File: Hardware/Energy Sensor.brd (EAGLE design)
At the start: 159 x 63 mm, 41 parts, among them Q1 16MHz

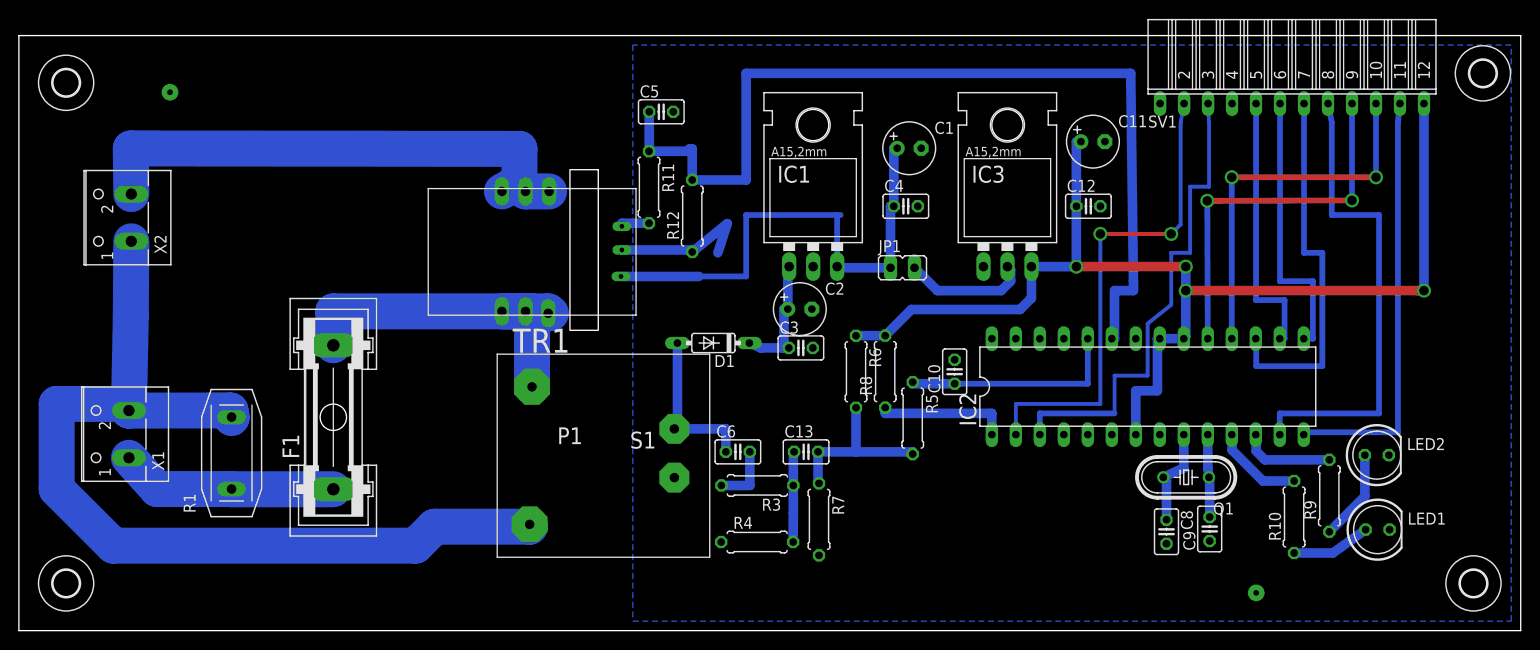
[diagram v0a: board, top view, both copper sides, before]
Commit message: update schematics, added switchmode psu to heating controller. fixed line endings for existing files
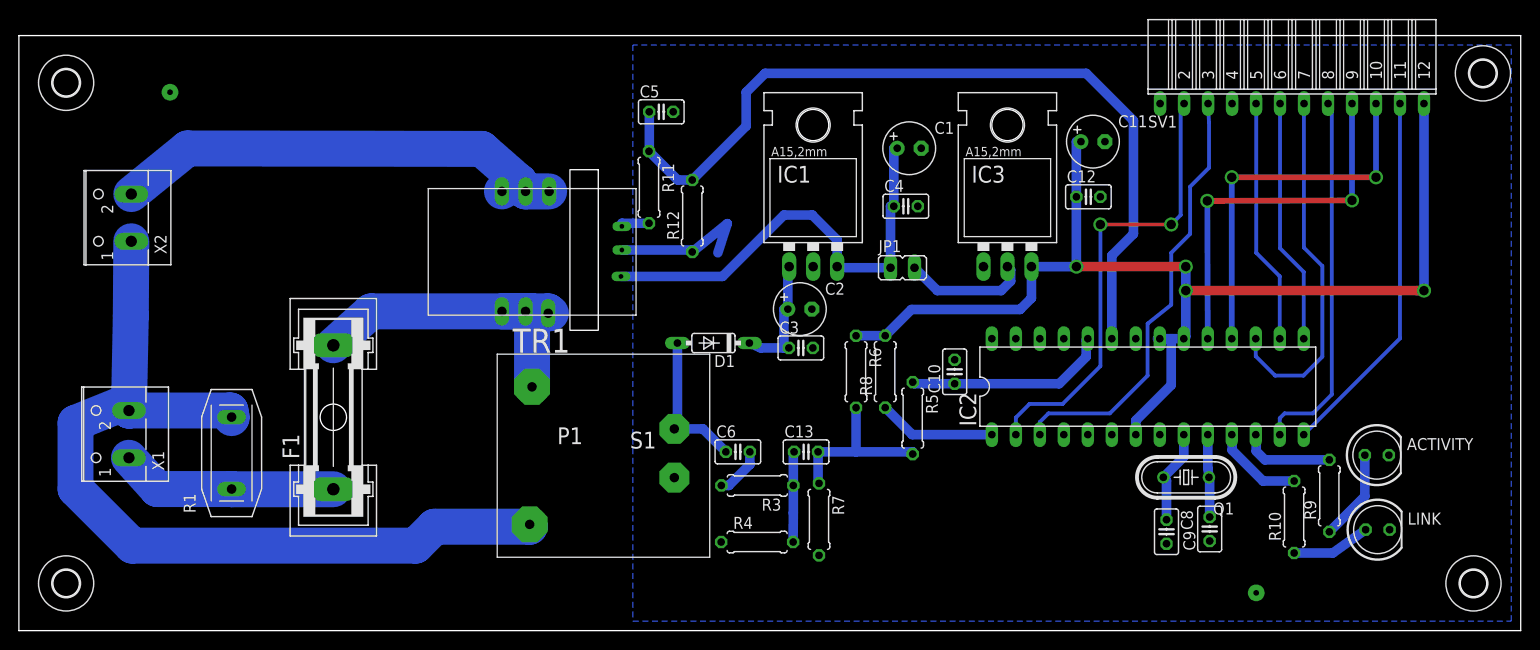
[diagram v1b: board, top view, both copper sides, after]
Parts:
- ACTIVITY: value (none) -> RED
- F1: value (none) -> 230V 10A
- IC1: value (none) -> 7805
- IC2: value (none) -> ATMega328p-pu
- IC3: value (none) -> ld33v
- JP1: value (none) -> Extern_Power
- LINK: value (none) -> GRN
- R10, R9: value (none) -> 330R
- R8: value (none) -> 10K
- SV1: value (none) -> Comms
- TR1: value (none) -> vn20.10 09477
- X1: value (none) -> MAINS IN
- X2: value (none) -> MAINS OUT
- moved C12 1.00 mm to (113.2, 45.9)
- renumbered LED1 to LINK, LED2 to ACTIVITY
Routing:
- net INT: track 50.6 -> 39.3 mm
- net CURRENT_SENSE: track 100.4 -> 89.6 mm
- net CSN2: track 45.0 -> 39.3 mm
- net +5V: track 54.6 -> 48.9 mm
- net N$2: track 100.1 -> 94.5 mm
- net N$8: track 55.3 -> 49.9 mm
- net TXD: track 51.7 -> 46.4 mm
- net CSN: track 29.3 -> 25.9 mm
- net RXD: track 51.9 -> 48.8 mm
- net CE: track 28.4 -> 25.9 mm
- net N$6: track 38.0 -> 35.8 mm
- net VSENSE: track 23.7 -> 21.6 mm
- net N$16: track 14.2 -> 12.5 mm
- net MOSI: track 39.7 -> 38.2 mm
- net N$5: track 17.3 -> 15.9 mm
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
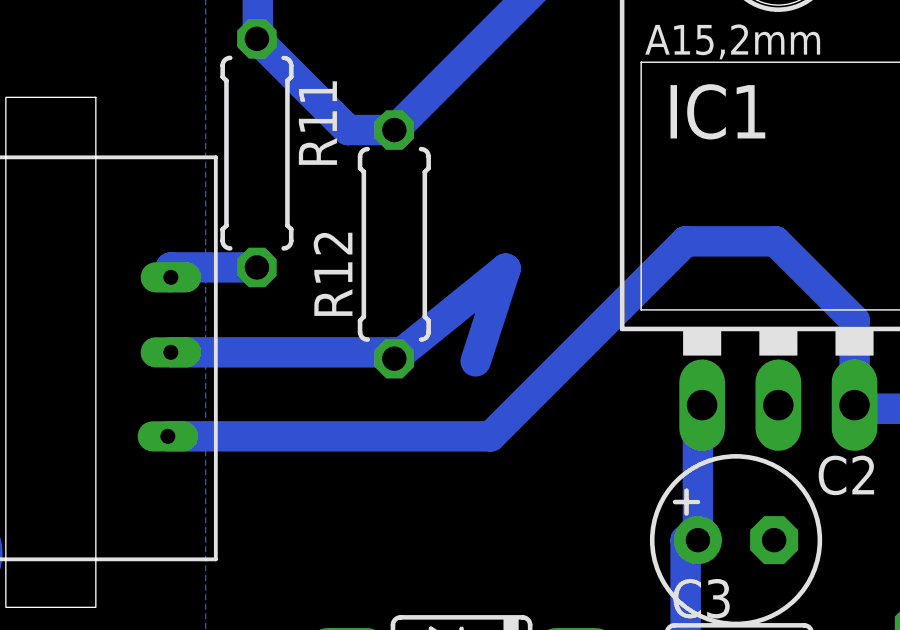
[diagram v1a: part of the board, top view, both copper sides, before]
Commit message: moved eagle custom parts to repo to allow for easier portability when working on designs
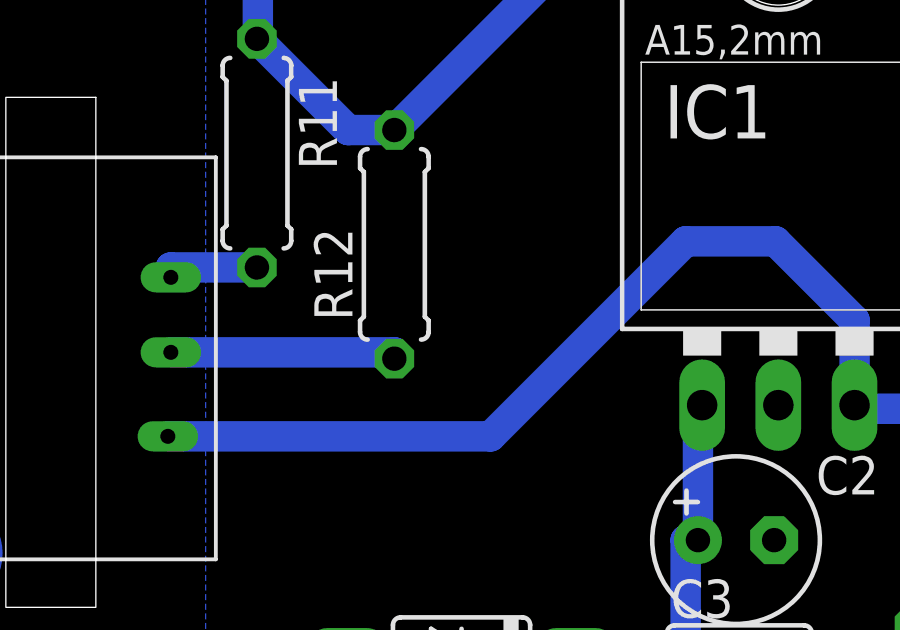
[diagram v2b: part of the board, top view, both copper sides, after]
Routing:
- net GND: track 15.9 -> 7.86 mm
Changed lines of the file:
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@@
 <?xml version="1.0" encoding="utf-8"?>
 <!DOCTYPE eagle SYSTEM "eagle.dtd">
-<eagle version="6.4">
+<eagle version="6.5.0">
 <drawing>
 <settings>
@@
 <wire x1="71.29" y1="40.09" x2="71.29" y2="40.3" width="1.016" layer="16"/>
 <wire x1="71.29" y1="40.3" x2="63.84" y2="40.3" width="1.016" layer="16"/>
-<wire x1="71.29" y1="40.09" x2="75" y2="43.09" width="1.016" layer="16"/>
-<wire x1="75" y1="43.09" x2="74" y2="40" width="1.016" layer="16"/>
 </signal>
 <signal name="+5V">

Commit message: updated fuse locations and updated missing values
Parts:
- added F2: 230V 100mA, fuse:GSH15
- moved F1 1.31 mm to (32.7, 21.4), turned to 270 degrees
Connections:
- removed net N$1: F1.1, R1.2, X1.1
- new net N$19: F2.2, R1.2, TR1.1
- new net N$22: F1.2, F2.1, X1.1
- net N$6: now also F1.1; no longer F1.2, TR1.1
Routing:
- net N$1: track 23.1 -> 0.00 mm
- net N$2: track 94.5 -> 78.3 mm
- net N$22: track 0.00 -> 14.9 mm
- net N$19: track 0.00 -> 9.41 mm
- net N$6: track 35.8 -> 29.1 mm
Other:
- board text removed: "230V 10A"
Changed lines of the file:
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@@
 <text x="3" y="40" size="1.778" layer="48">N</text>
 <text x="3.6" y="22.25" size="1.778" layer="48">N</text>
-<text x="41" y="16" size="1.778" layer="48" rot="R90">230V 10A</text>
 <text x="3" y="27" size="1.778" layer="48">MAINS</text>
 <text x="2" y="50" size="1.778" layer="48">OUTPUT</text>
@@
 </element>
 <element name="R1" library="varistor" package="P594" value="P594" x="22.52" y="18.8"/>
-<element name="F1" library="fuse" package="GSH15" value="230V 10A" x="33.29" y="22.59" rot="R90">
-<attribute name="OC_NEWARK" value="02P0318" x="85.36" y="81.01" size="1.778" layer="27" rot="R90" display="off"/>
-<attribute name="MPN" value="64900001039" x="85.36" y="81.01" size="1.778" layer="27" rot="R90" display="off"/>
-<attribute name="MF" value="" x="85.36" y="81.01" size="1.778" layer="27" rot="R90" display="off"/>
-<attribute name="OC_FARNELL" value="1271673" x="85.36" y="81.01" size="1.778" layer="27" rot="R90" display="off"/>
+<element name="F1" library="fuse" package="GSH15" value="230V 10A" x="32.71" y="21.41" rot="R270">
+<attribute name="OC_NEWARK" value="02P0318" x="-19.36" y="-37.01" size="1.778" layer="27" rot="R270" display="off"/>
+<attribute name="MPN" value="64900001039" x="-19.36" y="-37.01" size="1.778" layer="27" rot="R270" display="off"/>
+<attribute name="MF" value="" x="-19.36" y="-37.01" size="1.778" layer="27" rot="R270" display="off"/>
+<attribute name="OC_FARNELL" value="1271673" x="-19.36" y="-37.01" size="1.778" layer="27" rot="R270" display="off"/>
 </element>
 <element name="TR1" library="xformer" package="VV11" value="vn20.10 09477" x="50.64" y="7.77"/>
@@
 <element name="H3" library="holes" package="2,8" value="MOUNT-HOLE2.8" x="154" y="5"/>
 <element name="H4" library="holes" package="2,8" value="MOUNT-HOLE2.8" x="155" y="59"/>
+<element name="F2" library="fuse" package="GSH15" value="230V 100mA" x="45" y="18" rot="R90">
+<attribute name="OC_NEWARK" value="02P0318" x="45" y="18" size="1.778" layer="27" rot="R90" display="off"/>
+<attribute name="MPN" value="64900001039" x="45" y="18" size="1.778" layer="27" rot="R90" display="off"/>
+<attribute name="MF" value="" x="45" y="18" size="1.778" layer="27" rot="R90" display="off"/>
+<attribute name="OC_FARNELL" value="1271673" x="45" y="18" size="1.778" layer="27" rot="R90" display="off"/>
+</element>
 </elements>
 <signals>
-<signal name="N$1">
-<contactref element="X1" pad="1"/>
-<contactref element="F1" pad="1"/>
-<contactref element="R1" pad="2"/>
-<wire x1="11.65" y1="18.3" x2="14.65" y2="14.99" width="3.81" layer="16"/>
-<wire x1="14.65" y1="14.99" x2="22.52" y2="14.99" width="3.81" layer="16"/>
-<wire x1="22.52" y1="14.99" x2="22.52" y2="14.97" width="3.81" layer="16"/>
-<wire x1="22.52" y1="14.97" x2="33.29" y2="14.97" width="3.81" layer="16"/>
-</signal>
 <signal name="N$2">
-<contactref element="X1" pad="2"/>
 <contactref element="X2" pad="1"/>
 <wire x1="11.9" y1="41.22" x2="11.85" y2="33.35" width="3.81" layer="16"/>
-<wire x1="11.85" y1="33.35" x2="11.65" y2="23.3" width="3.81" layer="16"/>
-<contactref element="R1" pad="1"/>
-<wire x1="11.65" y1="23.3" x2="22.4" y2="23.31" width="3.81" layer="16"/>
-<wire x1="22.4" y1="23.31" x2="22.52" y2="22.61" width="3.81" layer="16"/>
 <contactref element="TR1" pad="5"/>
-<wire x1="22.52" y1="22.61" x2="22.52" y2="22.5" width="3.81" layer="16"/>
 <wire x1="54.077" y1="11.247" x2="54.077" y2="11" width="3.81" layer="16"/>
-<wire x1="54.077" y1="11" x2="44" y2="11" width="3.81" layer="16"/>
-<wire x1="44" y1="11" x2="42" y2="9" width="3.81" layer="16"/>
-<wire x1="42" y1="9" x2="12" y2="9" width="3.81" layer="16"/>
-<wire x1="12" y1="9" x2="6" y2="15" width="3.81" layer="16"/>
+<wire x1="54.077" y1="11" x2="51" y2="4" width="3.81" layer="16"/>
+<wire x1="51" y1="4" x2="15" y2="4" width="3.81" layer="16"/>
+<wire x1="15" y1="4" x2="6" y2="15" width="3.81" layer="16"/>
 <wire x1="6" y1="15" x2="6" y2="22" width="3.81" layer="16"/>
 <wire x1="6" y1="22" x2="10.95" y2="24" width="3.81" layer="16"/>
-<wire x1="10.95" y1="24" x2="11.65" y2="23.3" width="3.81" layer="16"/>
+<contactref element="R1" pad="1"/>
+<contactref element="X1" pad="2"/>
+<wire x1="10.95" y1="24" x2="11.85" y2="33.35" width="0" layer="19" extent="16-16"/>
+<wire x1="11.65" y1="23.3" x2="10.95" y2="24" width="0" layer="19" extent="16-16"/>
+<wire x1="22.52" y1="22.61" x2="11.65" y2="23.3" width="0" layer="19" extent="1-1"/>
 </signal>
 <signal name="N$5">
@@
 <contactref element="U$1" pad="2"/>
 <contactref element="U$1" pad="3"/>
-<contactref element="F1" pad="2"/>
 <wire x1="56.04" y1="33.6" x2="56.04" y2="33.8" width="3.81" layer="16"/>
 <wire x1="56.04" y1="33.8" x2="53.64" y2="33.8" width="3.81" layer="16"/>
 <wire x1="53.64" y1="33.8" x2="51.14" y2="33.8" width="3.81" layer="16"/>
 <wire x1="56.327" y1="33.6" x2="56.04" y2="33.6" width="3.81" layer="16"/>
-<wire x1="33.29" y1="30.21" x2="37.29" y2="33.8" width="3.81" layer="16"/>
 <wire x1="37.29" y1="33.8" x2="53.64" y2="33.8" width="3.81" layer="16"/>
-<contactref element="TR1" pad="1"/>
-<wire x1="54.327" y1="25.813" x2="54.327" y2="33.8" width="3.81" layer="16"/>
 <wire x1="54.327" y1="33.8" x2="53.64" y2="33.8" width="3.81" layer="16"/>
+<contactref element="F1" pad="1"/>
+<wire x1="32.71" y1="29.03" x2="32.71" y2="29.22" width="3.81" layer="16"/>
+<wire x1="32.71" y1="29.22" x2="37.29" y2="33.8" width="3.81" layer="16"/>
 </signal>
 <signal name="N$8">
@@
 <via x="16" y="57" extent="1-16" drill="0.6" diameter="1.778"/>
 </signal>
+<signal name="N$19">
+<contactref element="TR1" pad="1"/>
+<contactref element="F2" pad="2"/>
+<wire x1="45" y1="25.62" x2="54.134" y2="25.62" width="3.81" layer="16"/>
+<wire x1="54.134" y1="25.62" x2="54.327" y2="25.813" width="3.81" layer="16"/>
+<contactref element="R1" pad="2"/>
+<wire x1="22.52" y1="14.99" x2="45" y2="25.62" width="0" layer="19" extent="1-1"/>
+</signal>
+<signal name="N$22">
+<contactref element="X1" pad="1"/>
+<contactref element="F2" pad="1"/>
+<contactref element="F1" pad="2"/>
+<wire x1="32.71" y1="14.99" x2="32.71" y2="13.79" width="3.81" layer="16"/>
+<wire x1="32.71" y1="13.79" x2="41.59" y2="13.79" width="3.81" layer="16"/>
+<wire x1="41.59" y1="13.79" x2="45" y2="10.38" width="3.81" layer="16"/>
+<wire x1="11.65" y1="18.3" x2="32.71" y2="14.99" width="0" layer="19" extent="16-16"/>
+</signal>
 </signals>

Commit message: updated to fuse and varistor arrangements
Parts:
- moved R1 22.0 mm to (44.5, 17.2), turned to 180 degrees
- moved F1 11.7 mm to (21.7, 25.4)
- moved F2 11.0 mm to (34.0, 19.0)
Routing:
- net N$2: track 78.3 -> 103.4 mm
- net N$19: track 9.41 -> 24.6 mm
- net N$22: track 14.9 -> 25.2 mm
- net N$6: track 29.1 -> 38.3 mm
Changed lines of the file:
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@@
 <?xml version="1.0" encoding="utf-8"?>
 <!DOCTYPE eagle SYSTEM "eagle.dtd">
-<eagle version="6.5.0">
+<eagle version="6.4">
 <drawing>
 <settings>
@@
 <attribute name="OC_FARNELL" value="unknown" x="76.67" y="100.87" size="1.778" layer="27" rot="R90" display="off"/>
 </element>
-<element name="R1" library="varistor" package="P594" value="P594" x="22.52" y="18.8"/>
-<element name="F1" library="fuse" package="GSH15" value="230V 10A" x="32.71" y="21.41" rot="R270">
-<attribute name="OC_NEWARK" value="02P0318" x="-19.36" y="-37.01" size="1.778" layer="27" rot="R270" display="off"/>
-<attribute name="MPN" value="64900001039" x="-19.36" y="-37.01" size="1.778" layer="27" rot="R270" display="off"/>
-<attribute name="MF" value="" x="-19.36" y="-37.01" size="1.778" layer="27" rot="R270" display="off"/>
-<attribute name="OC_FARNELL" value="1271673" x="-19.36" y="-37.01" size="1.778" layer="27" rot="R270" display="off"/>
+<element name="R1" library="varistor" package="P594" value="P594" x="44.48" y="17.2" rot="R180"/>
+<element name="F1" library="fuse" package="GSH15" value="230V 10A" x="21.71" y="25.41" rot="R270">
+<attribute name="OC_NEWARK" value="02P0318" x="-30.36" y="-33.01" size="1.778" layer="27" rot="R270" display="off"/>
+<attribute name="MPN" value="64900001039" x="-30.36" y="-33.01" size="1.778" layer="27" rot="R270" display="off"/>
+<attribute name="MF" value="" x="-30.36" y="-33.01" size="1.778" layer="27" rot="R270" display="off"/>
+<attribute name="OC_FARNELL" value="1271673" x="-30.36" y="-33.01" size="1.778" layer="27" rot="R270" display="off"/>
 </element>
 <element name="TR1" library="xformer" package="VV11" value="vn20.10 09477" x="50.64" y="7.77"/>
@@
 <element name="H3" library="holes" package="2,8" value="MOUNT-HOLE2.8" x="154" y="5"/>
 <element name="H4" library="holes" package="2,8" value="MOUNT-HOLE2.8" x="155" y="59"/>
-<element name="F2" library="fuse" package="GSH15" value="230V 100mA" x="45" y="18" rot="R90">
-<attribute name="OC_NEWARK" value="02P0318" x="45" y="18" size="1.778" layer="27" rot="R90" display="off"/>
-<attribute name="MPN" value="64900001039" x="45" y="18" size="1.778" layer="27" rot="R90" display="off"/>
-<attribute name="MF" value="" x="45" y="18" size="1.778" layer="27" rot="R90" display="off"/>
-<attribute name="OC_FARNELL" value="1271673" x="45" y="18" size="1.778" layer="27" rot="R90" display="off"/>
+<element name="F2" library="fuse" package="GSH15" value="230V 100mA" x="34" y="19" rot="R90">
+<attribute name="OC_NEWARK" value="02P0318" x="34" y="19" size="1.778" layer="27" rot="R90" display="off"/>
+<attribute name="MPN" value="64900001039" x="34" y="19" size="1.778" layer="27" rot="R90" display="off"/>
+<attribute name="MF" value="" x="34" y="19" size="1.778" layer="27" rot="R90" display="off"/>
+<attribute name="OC_FARNELL" value="1271673" x="34" y="19" size="1.778" layer="27" rot="R90" display="off"/>
 </element>
 </elements>
@@
 <signal name="N$2">
 <contactref element="X2" pad="1"/>
-<wire x1="11.9" y1="41.22" x2="11.85" y2="33.35" width="3.81" layer="16"/>
 <contactref element="TR1" pad="5"/>
-<wire x1="54.077" y1="11.247" x2="54.077" y2="11" width="3.81" layer="16"/>
-<wire x1="54.077" y1="11" x2="51" y2="4" width="3.81" layer="16"/>
-<wire x1="51" y1="4" x2="15" y2="4" width="3.81" layer="16"/>
-<wire x1="15" y1="4" x2="6" y2="15" width="3.81" layer="16"/>
-<wire x1="6" y1="15" x2="6" y2="22" width="3.81" layer="16"/>
-<wire x1="6" y1="22" x2="10.95" y2="24" width="3.81" layer="16"/>
 <contactref element="R1" pad="1"/>
 <contactref element="X1" pad="2"/>
-<wire x1="10.95" y1="24" x2="11.85" y2="33.35" width="0" layer="19" extent="16-16"/>
-<wire x1="11.65" y1="23.3" x2="10.95" y2="24" width="0" layer="19" extent="16-16"/>
-<wire x1="22.52" y1="22.61" x2="11.65" y2="23.3" width="0" layer="19" extent="1-1"/>
+<wire x1="54.077" y1="11.247" x2="46.623" y2="11.247" width="3.81" layer="16"/>
+<wire x1="46.623" y1="11.247" x2="44.48" y2="13.39" width="3.81" layer="16"/>
+<wire x1="44.48" y1="13.39" x2="44.48" y2="9.48" width="3.81" layer="16"/>
+<wire x1="44.48" y1="9.48" x2="39" y2="4" width="3.81" layer="16"/>
+<wire x1="39" y1="4" x2="19" y2="4" width="3.81" layer="16"/>
+<wire x1="19" y1="4" x2="11" y2="12" width="3.81" layer="16"/>
+<wire x1="11" y1="12" x2="5" y2="12" width="3.81" layer="16"/>
+<wire x1="5" y1="12" x2="3" y2="14" width="3.81" layer="16"/>
+<wire x1="3" y1="14" x2="3" y2="27" width="3.81" layer="16"/>
+<wire x1="3" y1="27" x2="6" y2="30" width="3.81" layer="16"/>
+<wire x1="6" y1="30" x2="6.5" y2="29.5" width="3.81" layer="16"/>
+<wire x1="6.5" y1="29.5" x2="12" y2="24" width="3.81" layer="16"/>
+<wire x1="12" y1="24" x2="12" y2="23" width="3.81" layer="16"/>
+<wire x1="12" y1="23" x2="11.7" y2="23.3" width="3.81" layer="16"/>
+<wire x1="11.7" y1="23.3" x2="11.65" y2="23.3" width="3.81" layer="16"/>
+<wire x1="11.9" y1="41.22" x2="6.5" y2="35.82" width="3.81" layer="16"/>
+<wire x1="6.5" y1="35.82" x2="6.5" y2="29.5" width="3.81" layer="16"/>
 </signal>
 <signal name="N$5">
@@
 <wire x1="53.64" y1="33.8" x2="51.14" y2="33.8" width="3.81" layer="16"/>
 <wire x1="56.327" y1="33.6" x2="56.04" y2="33.6" width="3.81" layer="16"/>
-<wire x1="37.29" y1="33.8" x2="53.64" y2="33.8" width="3.81" layer="16"/>
+<wire x1="37.29" y1="33.8" x2="39" y2="33.8" width="3.81" layer="16"/>
+<wire x1="39" y1="33.8" x2="53.64" y2="33.8" width="3.81" layer="16"/>
 <wire x1="54.327" y1="33.8" x2="53.64" y2="33.8" width="3.81" layer="16"/>
 <contactref element="F1" pad="1"/>
-<wire x1="32.71" y1="29.03" x2="32.71" y2="29.22" width="3.81" layer="16"/>
-<wire x1="32.71" y1="29.22" x2="37.29" y2="33.8" width="3.81" layer="16"/>
+<wire x1="21.71" y1="33.03" x2="22.48" y2="33.8" width="3.81" layer="16"/>
+<wire x1="22.48" y1="33.8" x2="37.29" y2="33.8" width="3.81" layer="16"/>
 </signal>
 <signal name="N$8">
@@
 <contactref element="TR1" pad="1"/>
 <contactref element="F2" pad="2"/>
-<wire x1="45" y1="25.62" x2="54.134" y2="25.62" width="3.81" layer="16"/>
-<wire x1="54.134" y1="25.62" x2="54.327" y2="25.813" width="3.81" layer="16"/>
 <contactref element="R1" pad="2"/>
-<wire x1="22.52" y1="14.99" x2="45" y2="25.62" width="0" layer="19" extent="1-1"/>
+<wire x1="54.327" y1="25.813" x2="49.283" y2="25.813" width="3.81" layer="16"/>
+<wire x1="49.283" y1="25.813" x2="44.48" y2="21.01" width="3.81" layer="16"/>
+<wire x1="44.48" y1="21.01" x2="39.61" y2="21.01" width="3.81" layer="16"/>
+<wire x1="39.61" y1="21.01" x2="34" y2="26.62" width="3.81" layer="16"/>
 </signal>
 <signal name="N$22">
@@
 <contactref element="F2" pad="1"/>
 <contactref element="F1" pad="2"/>
-<wire x1="32.71" y1="14.99" x2="32.71" y2="13.79" width="3.81" layer="16"/>
-<wire x1="32.71" y1="13.79" x2="41.59" y2="13.79" width="3.81" layer="16"/>
-<wire x1="41.59" y1="13.79" x2="45" y2="10.38" width="3.81" layer="16"/>
-<wire x1="11.65" y1="18.3" x2="32.71" y2="14.99" width="0" layer="19" extent="16-16"/>
+<wire x1="34" y1="11.38" x2="27.59" y2="17.79" width="3.81" layer="16"/>
+<wire x1="27.59" y1="17.79" x2="21.71" y2="17.79" width="3.81" layer="16"/>
+<wire x1="21.71" y1="17.79" x2="21.2" y2="18.3" width="3.81" layer="16"/>
+<wire x1="21.2" y1="18.3" x2="11.65" y2="18.3" width="3.81" layer="16"/>
 </signal>
 </signals>
